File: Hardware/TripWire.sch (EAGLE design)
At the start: 69 parts, among them P1 LSP11, P2 LSP11, P3 LSP11, P4 LSP11, P5 LSP11, P6 LSP11, P7 LSP11, X1 GADGETEER-SOCKET

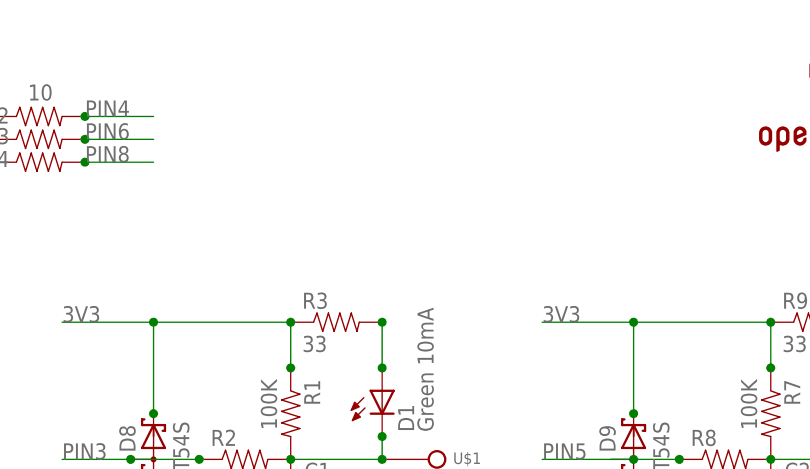
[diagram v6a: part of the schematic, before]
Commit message: Created BAT54SDW diode array part.
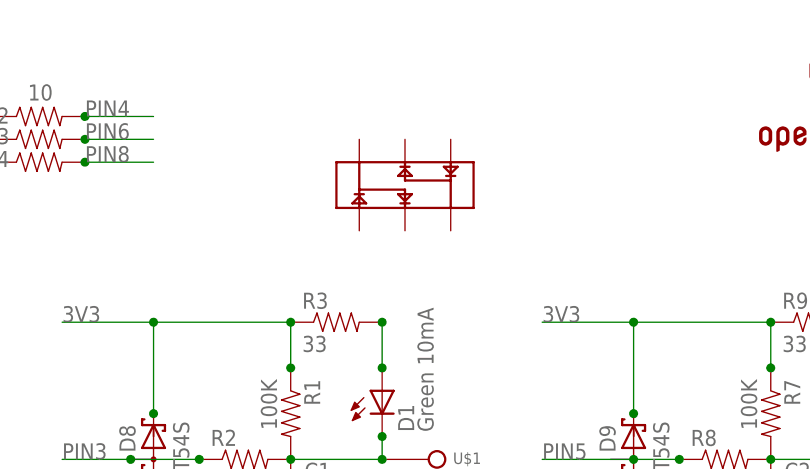
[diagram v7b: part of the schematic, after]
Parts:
- added U$9: BAT54SDW, SoftDust:BAT54SDW
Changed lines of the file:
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@@
 <?xml version="1.0" encoding="utf-8"?>
 <!DOCTYPE eagle SYSTEM "eagle.dtd">
-<eagle version="6.1">
+<eagle version="6.4">
 <drawing>
 <settings>
@@
 <part name="C7" library="SparkFun-Capacitors" deviceset="CAP" device="0603-CAP" value="0.01 uF"/>
 <part name="GND9" library="supply1" deviceset="GND" device=""/>
+<part name="U$9" library="SoftDust" deviceset="BAT54SDW" device=""/>
 </parts>
 <sheets>
@@
 <instance part="C7" gate="G$1" x="33.02" y="12.7"/>
 <instance part="GND9" gate="1" x="33.02" y="7.62"/>
+<instance part="U$9" gate="G$1" x="116.84" y="109.22"/>
 </instances>
 <busses>
@@
 </schematic>
 </drawing>
+<compatibility>
+<note version="6.3" minversion="6.2.2" severity="warning">
+Since Version 6.2.2 text objects can contain more than one line,
+which will not be processed correctly with this version.
+</note>
+</compatibility>
 </eagle>

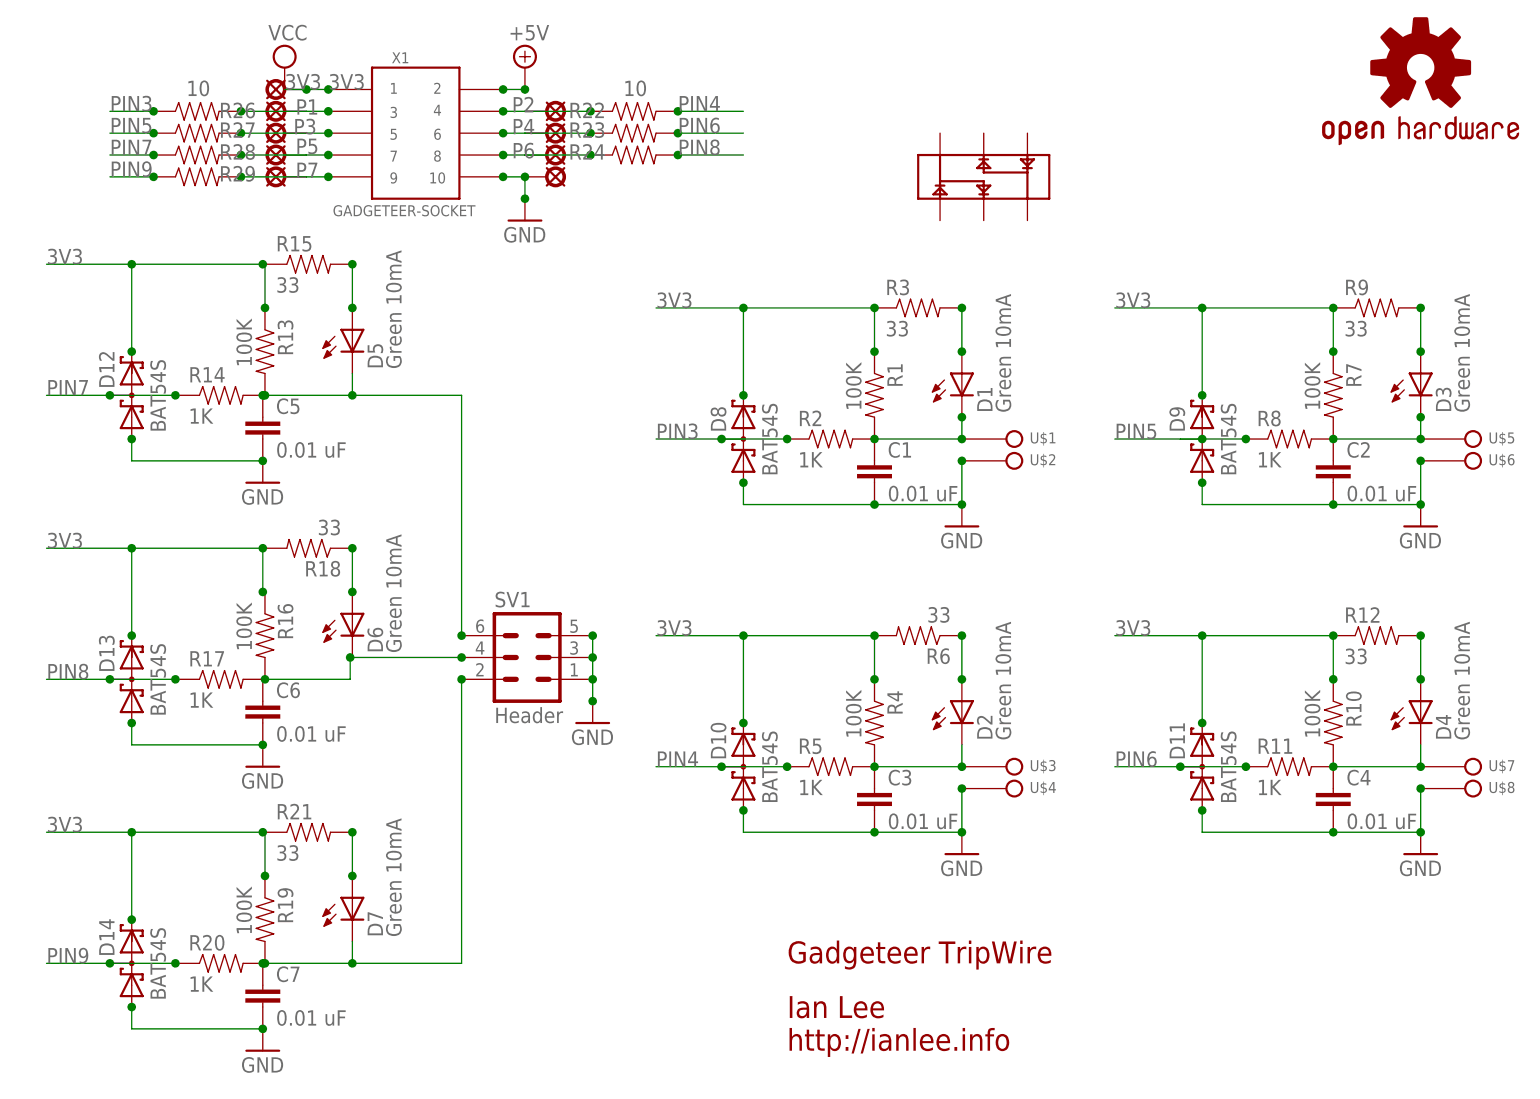
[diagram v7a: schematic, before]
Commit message: Replaced all transistor pairs with BAT54SDW diode arrays.
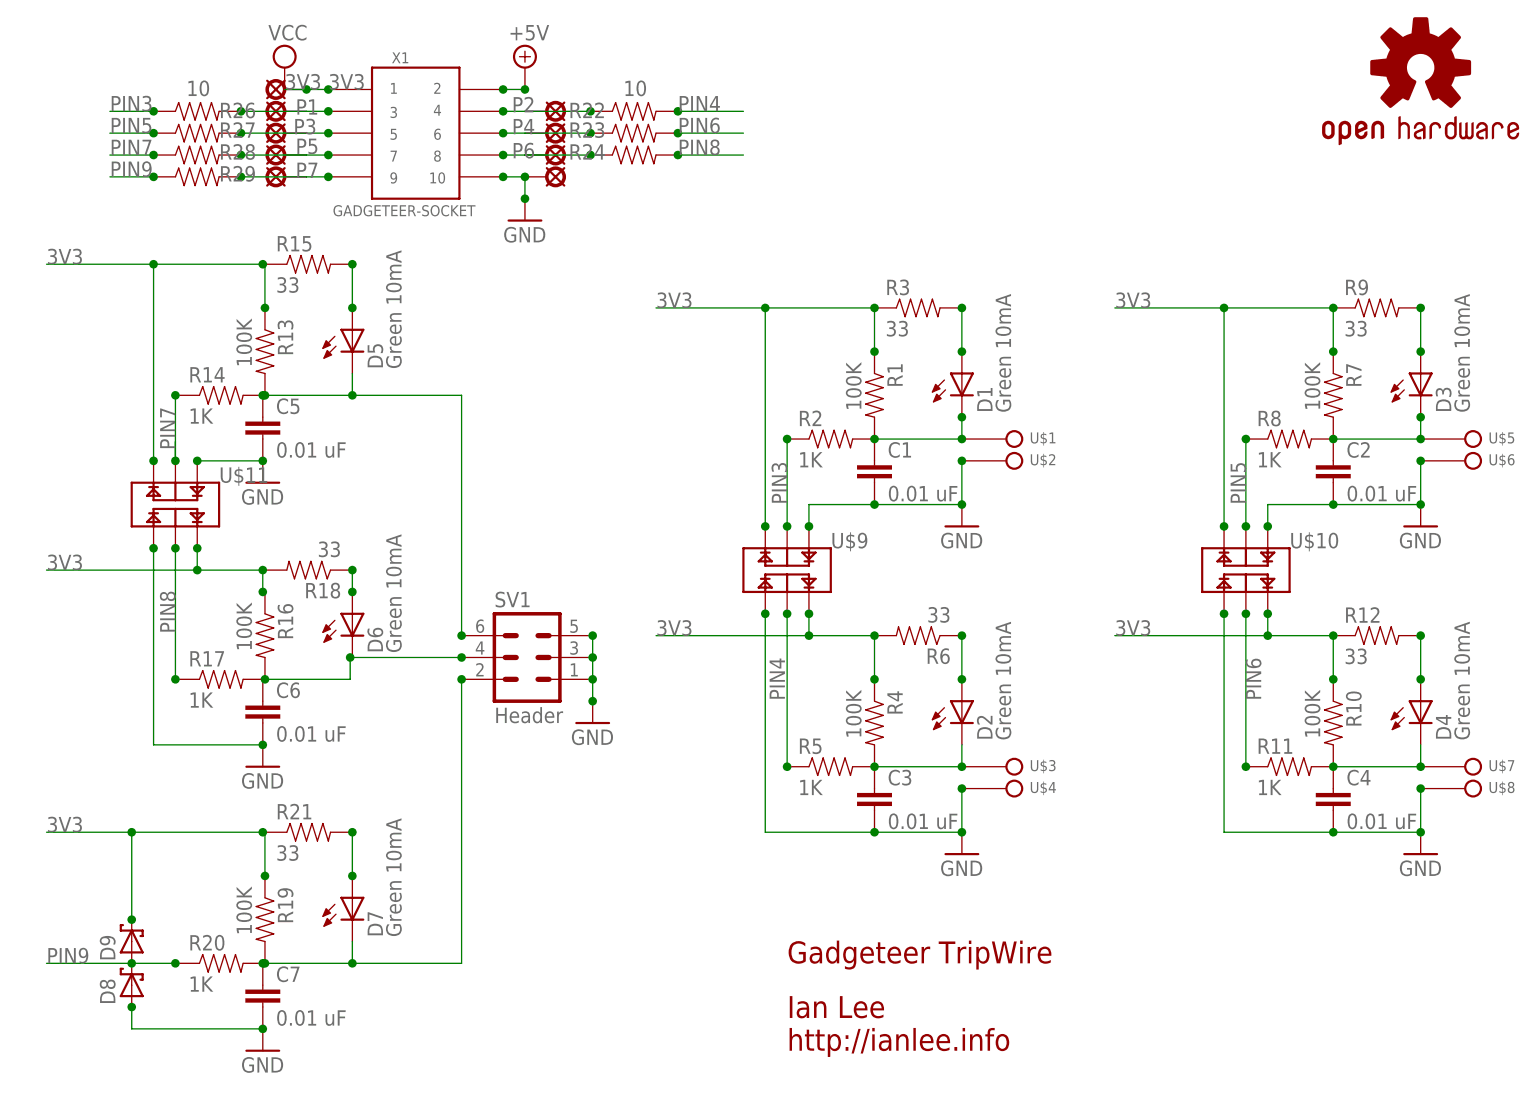
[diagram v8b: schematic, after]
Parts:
- removed D10, D11, D12, D13, D14: BAT54S, diode:BAT54S
- added U$10, U$11: BAT54SDW, SoftDust:BAT54SDW
- D8, D9: value BAT54S -> (none); device diode:BAT54S -> diode:SCHOTTKY-DIODESMD
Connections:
- net 3V3: now also D9.C, U$10.C1, U$10.C2, U$11.C1, U$11.C2, U$9.C1, U$9.C2; no longer D10.C2, D11.C2, D12.C2, D13.C2, D14.C2, D8.C2, D9.C2
- net GND: now also D8.A, U$10.A1, U$10.A2, U$11.A1, U$11.A2, U$9.A1, U$9.A2; no longer D10.A1, D11.A1, D12.A1, D13.A1, D14.A1, D8.A1, D9.A1
- net PIN3: now also U$9.AC2; no longer D8.C1A2
- net PIN4: now also U$9.AC1; no longer D10.C1A2
- net PIN5: now also U$10.AC2; no longer D9.C1A2
- net PIN6: now also U$10.AC1; no longer D11.C1A2
- net PIN7: now also U$11.AC2; no longer D12.C1A2
- net PIN8: now also U$11.AC1; no longer D13.C1A2
- net PIN9: now also D8.C, D9.A; no longer D14.C1A2
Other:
- moved on the sheet: R18
